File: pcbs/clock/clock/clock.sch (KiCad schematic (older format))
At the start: 39 parts, among them J1 USB_B_Micro, Q1 BSS138, Q2 BSS138, SW1 SW_Push, U1 USBLC6-2SC6, U2 AP2112K-3.3, U3 SAMD21Exx, U4 PCF85263ATT, U5 TCA6416APWR, U6 AT24CS01-SSHM, Y1 32.768k

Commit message: Rough clock layout.
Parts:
- added R37, R38: 2.2k, Resistor_SMD:R_0603_1608Metric, symbol Device:R_Small
- BT1: footprint (none) -> Battery:BatteryHolder_Keystone_3034_1x20mm
- C1, C10, C11, C12, C13, C14, C2, C3, C4, C5, C6, C7, C8, C9: footprint (none) -> Capacitor_SMD:C_0603_1608Metric
- D1, D2, D3, D4: footprint (none) -> LED_SMD:LED_0603_1608Metric
- FB1: footprint (none) -> Inductor_SMD:L_0603_1608Metric
- J1: footprint (none) -> Connector_USB:USB_Micro-B_Amphenol_10103594-0001LF_Horizontal
- R1, R2, R3, R4, R5, R6, R7, R8: footprint (none) -> Resistor_SMD:R_0603_1608Metric
- SW1: footprint (none) -> Button_Switch_SMD:SW_SPST_PTS645
- U3: footprint (none) -> Package_DFN_QFN:QFN-32-1EP_5x5mm_P0.5mm_EP3.6x3.6mm; symbol matir-kicad:SAMD21Exx -> clock-rescue:SAMD21Exx-QFN
- U4: footprint (none) -> Package_SO:TSSOP-8_3x3mm_P0.65mm; symbol matir-kicad:PCF85263ATT -> clock-rescue:PCF85263ATT-matir-kicad
- U5: footprint (none) -> Package_SO:TSSOP-24_4.4x7.8mm_P0.65mm; symbol matir-kicad:TCA6416APWR -> clock-rescue:TCA6416APWR-matir-kicad
- Y1: footprint (none) -> Crystal:Crystal_SMD_MicroCrystal_CC7V-T1A-2Pin_3.2x1.5mm
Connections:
- net +3V3: now also R37.1, R38.1
- net GND: now also U3.33 (PAD_GND)
- net SCL: now also R37.2
- net SDA: now also R38.2
- net USB_N: now also U1.6 (I/O1); no longer U1.4 (I/O2)
- net USB_P: now also U1.4 (I/O2); no longer U1.6 (I/O1)
- net at J1.2 (D-): now also U1.1 (I/O1); no longer U1.3 (I/O2)
- net at J1.3 (D+): now also U1.3 (I/O2); no longer U1.1 (I/O1)
- net Displays/SEGA renamed Displays/SEG_A
- net Displays/SEGB renamed Displays/SEG_B
- net Displays/SEGC renamed Displays/SEG_C
- net Displays/SEGD renamed Displays/SEG_D
- net Displays/SEGDP renamed Displays/SEG_DP
- net Displays/SEGE renamed Displays/SEG_E
- net Displays/SEGF renamed Displays/SEG_F
- net Displays/SEGG renamed Displays/SEG_G

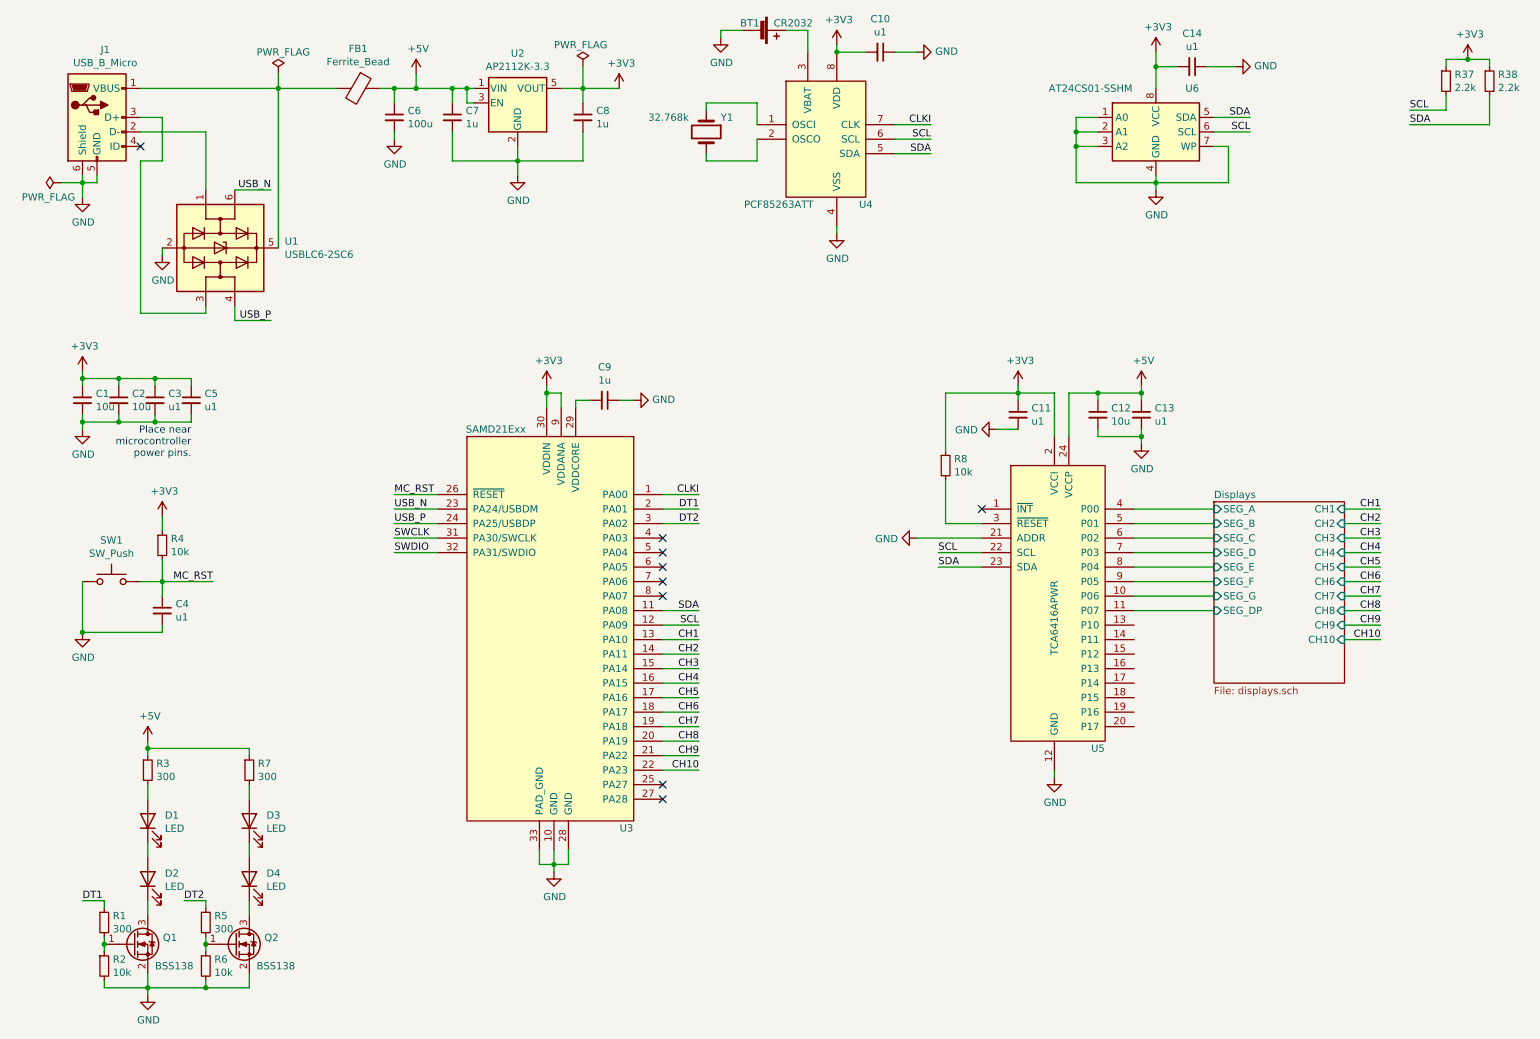
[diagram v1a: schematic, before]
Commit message: Start clock layout
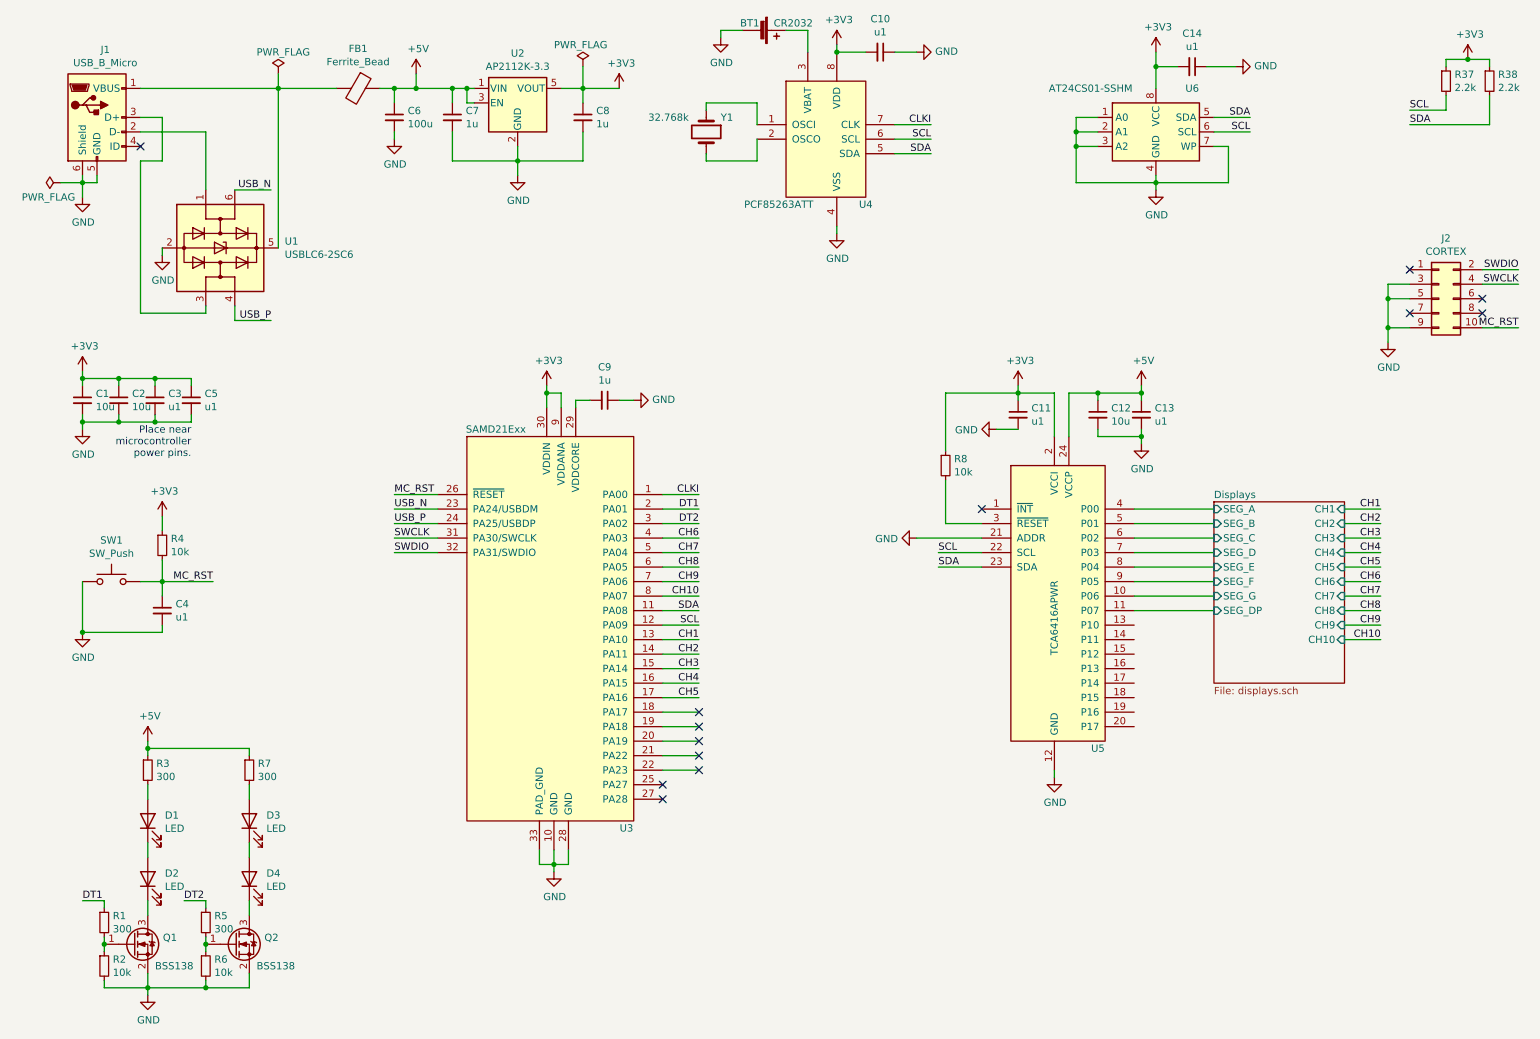
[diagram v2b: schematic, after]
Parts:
- added J2: CORTEX, Connector_PinHeader_1.27mm:PinHeader_2x05_P1.27mm_Vertical_SMD, symbol Connector_Generic:Conn_02x05_Odd_Even
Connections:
- net CH10: now also U3.8 (PA07); no longer U3.22 (PA23)
- net CH6: now also U3.4 (PA03); no longer U3.18 (PA17)
- net CH7: now also U3.5 (PA04); no longer U3.19 (PA18)
- net CH8: now also U3.6 (PA05); no longer U3.20 (PA19)
- net CH9: now also U3.7 (PA06); no longer U3.21 (PA22)
- net GND: now also J2.3 (Pin_3), J2.5 (Pin_5), J2.9 (Pin_9)
- net MC_RST: now also J2.10 (Pin_10)
- net SWCLK: now also J2.4 (Pin_4)
- net SWDIO: now also J2.2 (Pin_2)
- no-connect marks 9 -> 13
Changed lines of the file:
@@
 Text Label 5100 5250 2    50   ~ 0
 CH5
-Text Label 5100 5350 2    50   ~ 0
+Text Label 5100 4150 2    50   ~ 0
 CH6
-Text Label 5100 5450 2    50   ~ 0
+Text Label 5100 4250 2    50   ~ 0
 CH7
-Text Label 5100 5550 2    50   ~ 0
+Text Label 5100 4350 2    50   ~ 0
 CH8
-Text Label 5100 5650 2    50   ~ 0
+Text Label 5100 4450 2    50   ~ 0
 CH9
-Text Label 5100 5750 2    50   ~ 0
+Text Label 5100 4550 2    50   ~ 0
 CH10
 $Comp
@@
 Wire Wire Line
 	7700 1450 7700 1700
-NoConn ~ 4850 4150
-NoConn ~ 4850 4250
-NoConn ~ 4850 4350
-NoConn ~ 4850 4450
-NoConn ~ 4850 4550
 NoConn ~ 4850 5850
 NoConn ~ 4850 5950
@@
 F19 "SEG_DP" I L 8650 4650 50
 $EndSheet
+Wire Wire Line
+	4850 4150 5100 4150
+Wire Wire Line
+	4850 4250 5100 4250
+Wire Wire Line
+	4850 4350 5100 4350
+Wire Wire Line
+	4850 4450 5100 4450
+Wire Wire Line
+	4850 4550 5100 4550
+NoConn ~ 5100 5350
+NoConn ~ 5100 5450
+NoConn ~ 5100 5550
+NoConn ~ 5100 5650
+NoConn ~ 5100 5750
+$Comp
+L Connector_Generic:Conn_02x05_Odd_Even J2
+U 1 1 600C746C
+P 10200 2500
+F 0 "J2" H 10250 2917 50  0000 C CNN
+F 1 "CORTEX" H 10250 2826 50  0000 C CNN
+F 2 "Connector_PinHeader_1.27mm:PinHeader_2x05_P1.27mm_Vertical_SMD" H 10200 2500 50  0001 C CNN
+F 3 "~" H 10200 2500 50  0001 C CNN
+	1    10200 2500
+	1    0    0    -1
+$EndComp
+Wire Wire Line
+	10500 2300 10750 2300
+Wire Wire Line
+	10500 2400 10750 2400
+Text Label 10750 2300 2    50   ~ 0
+SWDIO
+Text Label 10750 2400 2    50   ~ 0
+SWCLK
+Text Label 10750 2700 2    50   ~ 0
+MC_RST
+Wire Wire Line
+	10750 2700 10500 2700
+NoConn ~ 10000 2600
+NoConn ~ 10000 2300
+NoConn ~ 10500 2500
+NoConn ~ 10500 2600
+$Comp
+L power:GND #PWR040
+U 1 1 60121361
+P 9850 2800
+F 0 "#PWR040" H 9850 2550 50  0001 C CNN
+F 1 "GND" H 9855 2627 50  0000 C CNN
+F 2 "" H 9850 2800 50  0001 C CNN
+F 3 "" H 9850 2800 50  0001 C CNN
+	1    9850 2800
+	1    0    0    -1
+$EndComp
+Wire Wire Line
+	9850 2800 9850 2700
+Wire Wire Line
+	9850 2400 10000 2400
+Wire Wire Line
+	10000 2500 9850 2500
+Connection ~ 9850 2500
+Wire Wire Line
+	9850 2500 9850 2400
+Wire Wire Line
+	10000 2700 9850 2700
+Connection ~ 9850 2700
+Wire Wire Line
+	9850 2700 9850 2500
 $EndSCHEMATC

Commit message: Progress
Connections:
- net CH1: now also U3.4 (PA03); no longer U3.13 (PA10)
- net CH10: now also U3.17 (PA16); no longer U3.8 (PA07)
- net CH2: now also U3.5 (PA04); no longer U3.14 (PA11)
- net CH3: now also U3.6 (PA05); no longer U3.15 (PA14)
- net CH4: now also U3.7 (PA06); no longer U3.16 (PA15)
- net CH5: now also U3.8 (PA07); no longer U3.17 (PA16)
- net CH6: now also U3.13 (PA10); no longer U3.4 (PA03)
- net CH7: now also U3.14 (PA11); no longer U3.5 (PA04)
- net CH8: now also U3.15 (PA14); no longer U3.6 (PA05)
- net CH9: now also U3.16 (PA15); no longer U3.7 (PA06)
- net Displays/SEG_A: now also U5.6 (P02); no longer U5.4 (P00)
- net Displays/SEG_B: now also U5.7 (P03); no longer U5.5 (P01)
- net Displays/SEG_C: now also U5.18 (P15); no longer U5.6 (P02)
- net Displays/SEG_D: now also U5.19 (P16); no longer U5.7 (P03)
- net Displays/SEG_DP: now also U5.17 (P14); no longer U5.11 (P07)
- net Displays/SEG_E: now also U5.20 (P17); no longer U5.8 (P04)
- net Displays/SEG_F: now also U5.5 (P01); no longer U5.9 (P05)
- net Displays/SEG_G: now also U5.4 (P00); no longer U5.10 (P06)
- no-connect marks 13 -> 21
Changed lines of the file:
@@
 Wire Wire Line
 	8650 4050 8100 4050
-Wire Wire Line
-	8100 4150 8650 4150
-Wire Wire Line
-	8650 4250 8100 4250
-Wire Wire Line
-	8100 4350 8650 4350
-Wire Wire Line
-	8650 4450 8100 4450
-Wire Wire Line
-	8100 4550 8650 4550
-Wire Wire Line
-	8650 4650 8100 4650
 $Comp
 L power:GND #PWR023
@@
 Wire Wire Line
 	4850 5650 5100 5650
+Text Label 5100 4150 2    50   ~ 0
+CH1
+Text Label 5100 4250 2    50   ~ 0
+CH2
+Text Label 5100 4350 2    50   ~ 0
+CH3
+Text Label 5100 4450 2    50   ~ 0
+CH4
+Text Label 5100 4550 2    50   ~ 0
+CH5
 Text Label 5100 4850 2    50   ~ 0
-CH1
+CH6
 Text Label 5100 4950 2    50   ~ 0
-CH2
+CH7
 Text Label 5100 5050 2    50   ~ 0
-CH3
+CH8
 Text Label 5100 5150 2    50   ~ 0
-CH4
+CH9
 Text Label 5100 5250 2    50   ~ 0
-CH5
-Text Label 5100 4150 2    50   ~ 0
-CH6
-Text Label 5100 4250 2    50   ~ 0
-CH7
-Text Label 5100 4350 2    50   ~ 0
-CH8
-Text Label 5100 4450 2    50   ~ 0
-CH9
-Text Label 5100 4550 2    50   ~ 0
 CH10
 $Comp
@@
 SDA
 $Sheet
-S 8650 3900 900  1250
+S 8650 3900 900  1700
 U 5FED6B92
 F0 "Displays" 50
@@
 F10 "CH7" I R 9550 4550 50
 F11 "CH6" I R 9550 4450 50
-F12 "SEG_A" I L 8650 3950 50
-F13 "SEG_B" I L 8650 4050 50
-F14 "SEG_C" I L 8650 4150 50
-F15 "SEG_D" I L 8650 4250 50
-F16 "SEG_E" I L 8650 4350 50
-F17 "SEG_F" I L 8650 4450 50
-F18 "SEG_G" I L 8650 4550 50
-F19 "SEG_DP" I L 8650 4650 50
+F12 "SEG_A" I L 8650 4150 50
+F13 "SEG_B" I L 8650 4250 50
+F14 "SEG_C" I L 8650 5250 50
+F15 "SEG_D" I L 8650 5350 50
+F16 "SEG_E" I L 8650 5450 50
+F17 "SEG_F" I L 8650 4050 50
+F18 "SEG_G" I L 8650 3950 50
+F19 "SEG_DP" I L 8650 5150 50
 $EndSheet
 Wire Wire Line
@@
 Wire Wire Line
 	9850 2700 9850 2500
+Wire Wire Line
+	8100 4150 8650 4150
+Wire Wire Line
+	8100 4250 8650 4250
+Wire Wire Line
+	8650 5450 8100 5450
+Wire Wire Line
+	8100 5350 8650 5350
+Wire Wire Line
+	8650 5250 8100 5250
+Wire Wire Line
+	8100 5150 8650 5150
+NoConn ~ 8100 4350
+NoConn ~ 8100 4450
+NoConn ~ 8100 4550
+NoConn ~ 8100 4650
+NoConn ~ 8100 4750
+NoConn ~ 8100 4850
+NoConn ~ 8100 4950
+NoConn ~ 8100 5050
 $EndSCHEMATC
